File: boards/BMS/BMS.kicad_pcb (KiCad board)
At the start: 2 copper layers, 65 parts, among them IC1 ATMEGA16M1, J1 Mounting_Hole_4-40, J2 Mounting_Hole_4-40, J3 Mounting_Hole_4-40, J4 Ultrafit_4, J5 Mounting_Hole_4-40, J6 Ultrafit_4, J7 NanoFit_2, J8 Ultrafit_5, K1 G5Q-1A4-DC5-5V, P1 CONN_02X03, Q1 2N7002, T1 T_LAN_7490100111A, U1 micro-match12pin, U2 CAN_Transceiver, U3 TPS561201, U4 SN74LVC1G17, U5 AD623, U6 MCP6001, U7 LTC6820, Y1 Crystal_SMD

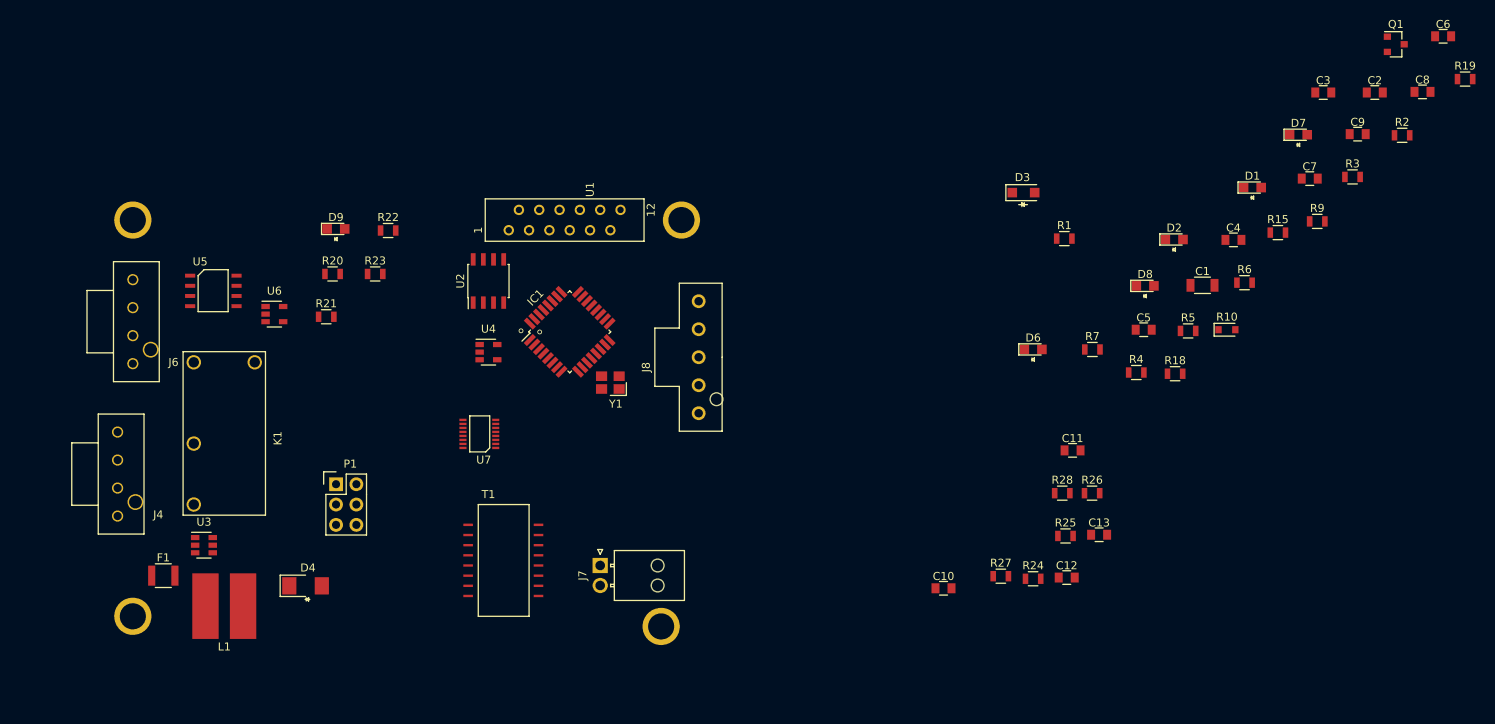
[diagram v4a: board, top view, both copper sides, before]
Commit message: BMS: Layout, tracing, and fabrication outputs
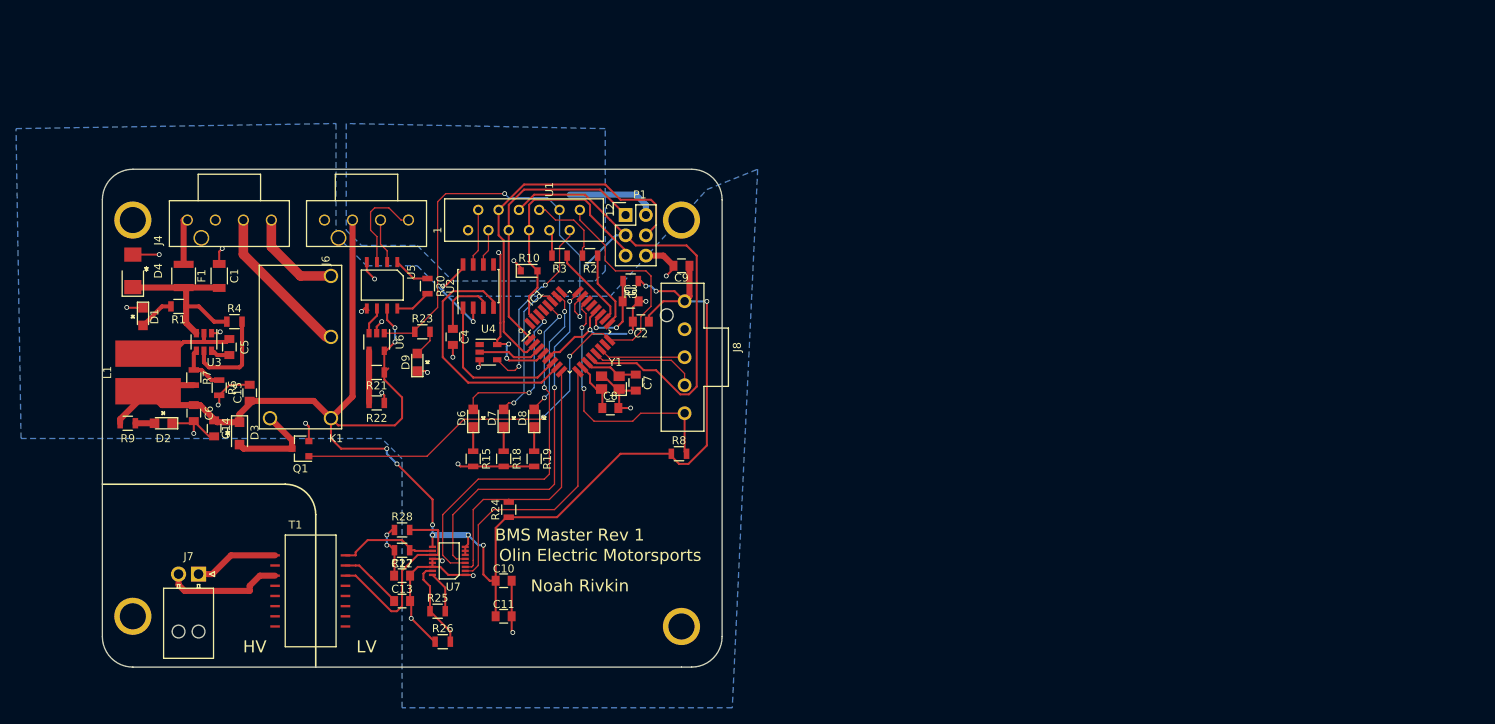
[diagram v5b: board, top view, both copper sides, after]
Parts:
- added C14: C_10uF_16V, footprints:C_0805_OEM, F.Cu at (138.4, 92.1)
- added C15: C_0.1uF, footprints:C_0805_OEM, F.Cu at (142.9, 87.6)
- added R8: R_10k, footprints:R_0805_OEM, F.Cu at (196.5, 95.2)
- moved C6 163.1 mm to (135.9, 90.2), turned to 270 degrees
- moved R9 150.8 mm to (127.6, 91.4)
- moved Q1 145.9 mm to (149.2, 94.6), turned to 180 degrees
- moved D1 139.6 mm to (129.5, 78.1), turned to 270 degrees
- moved R6 128.8 mm to (139.1, 87.0), turned to 270 degrees
- moved D2 128.4 mm to (132.1, 91.4), turned to 180 degrees
- moved R19 125.7 mm to (178.4, 95.9), turned to 270 degrees
- moved C1 122.9 mm to (139.1, 73.0), turned to 90 degrees
- moved C5 114.3 mm to (140.3, 81.9), turned to 90 degrees
- moved R4 112.9 mm to (141.0, 78.7)
- moved R7 112.4 mm to (135.9, 85.7), turned to 270 degrees
- moved R1 111.0 mm to (134.0, 76.8), turned to 180 degrees
- moved C8 108.9 mm to (188.0, 89.5)
- moved D7 105.5 mm to (174.6, 90.8), turned to 90 degrees
- moved R15 104.5 mm to (170.8, 95.9), turned to 270 degrees
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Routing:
- net VCC: track 0.00 -> 252.0 mm, vias 0 -> 15
- net GND: track 0.00 -> 118.0 mm, vias 0 -> 26
- net Shutdown_Control: track 0.00 -> 72.8 mm, vias 0 -> 2
- net SCK: track 0.00 -> 64.7 mm
- net BSPD_Current_Sense: track 0.00 -> 55.4 mm, vias 0 -> 2
- net MOSI: track 0.00 -> 47.2 mm
- net SCK_iso: track 0.00 -> 46.5 mm, vias 0 -> 2
- net CS_iso: track 0.00 -> 46.3 mm, vias 0 -> 2
- net MOSI_iso: track 0.00 -> 35.8 mm
- net MISO_iso: track 0.00 -> 35.0 mm
- net MISO: track 0.00 -> 34.7 mm
- net Net-(IC1-Pad22): track 0.00 -> 33.2 mm, vias 0 -> 2
- net RESET: track 0.00 -> 31.8 mm
- net RXCAN: track 0.00 -> 31.6 mm
- net Net-(R28-Pad2): track 0.00 -> 25.9 mm
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- added copper zone on B.Cu, net GND
- added copper zone on B.Cu, net VCC
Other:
- board outline added: 77.5 x 62.2 mm
- board text added: "BMS Master Rev 1"
- board text added: "HV"
- board text added: "LV"
- board text added: "Noah Rivkin"
- board text added: "Olin Electric Motorsports"

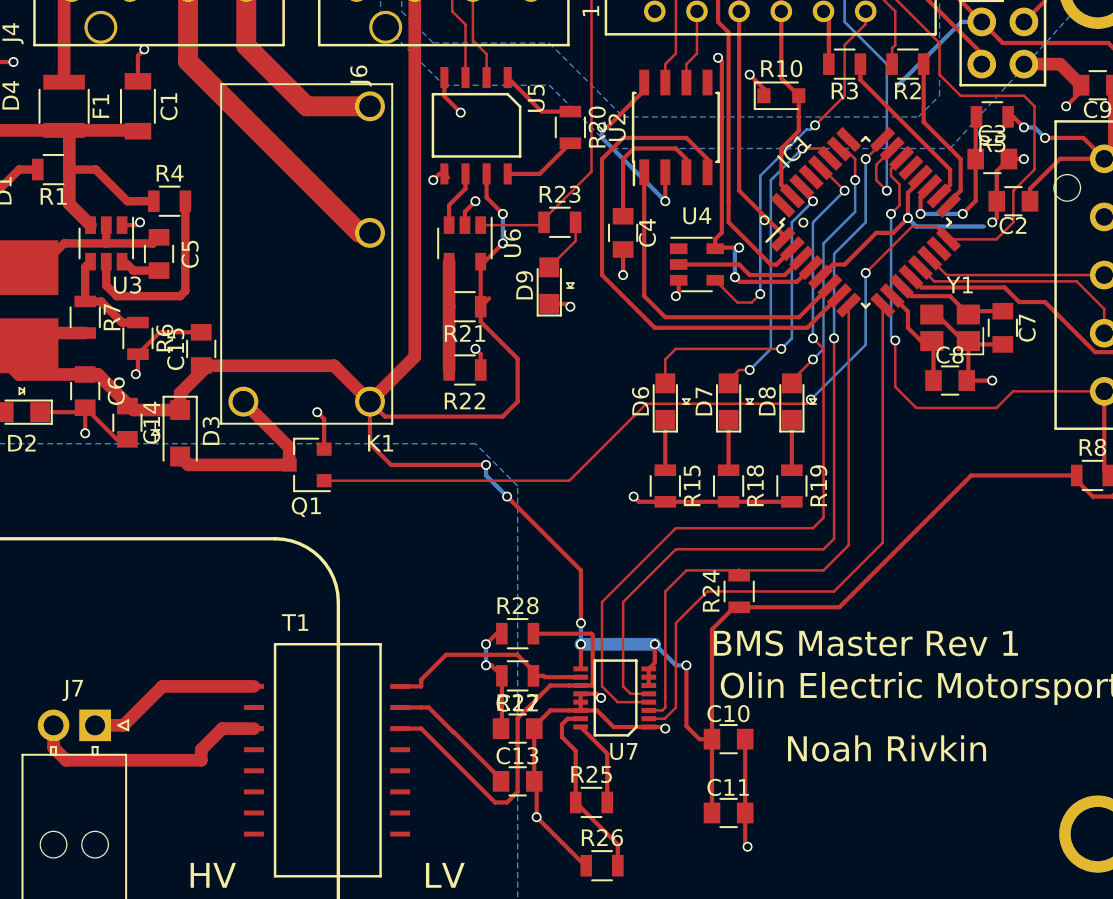
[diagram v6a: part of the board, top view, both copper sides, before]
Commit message: BMS_Slave: updated tracing/connector for temp sense
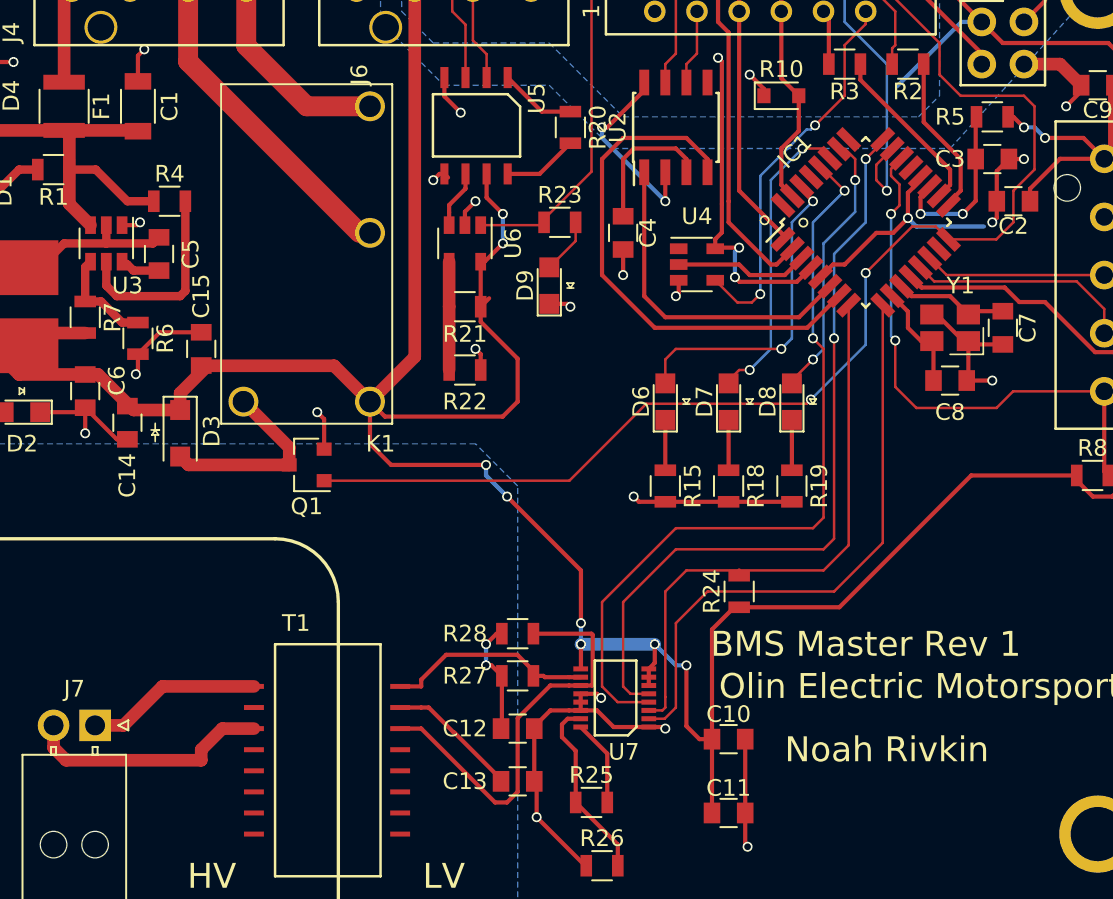
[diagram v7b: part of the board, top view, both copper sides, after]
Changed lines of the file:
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@@
     (links 155)
     (no_connects 0)
-    (area 124.384999 59.614999 202.005001 121.995001)
+    (area 113.665 53.975 206.375001 127.000001)
     (thickness 1.6)
     (drawings 24)
@@
     (tags "capacitor 0805")
     (attr smd)
-    (fp_text reference C3 (at 0 -1.5) (layer F.SilkS)
+    (fp_text reference C3 (at -2.54 0) (layer F.SilkS)
       (effects (font (size 1 1) (thickness 0.15)))
     )
@@
     (tags "capacitor 0805")
     (attr smd)
-    (fp_text reference C6 (at 0 -1.905 270) (layer F.SilkS)
+    (fp_text reference C6 (at -0.635 -1.905 270) (layer F.SilkS)
       (effects (font (size 1 1) (thickness 0.15)))
     )
@@
     (tags "capacitor 0805")
     (attr smd)
-    (fp_text reference C8 (at 0 -1.5) (layer F.SilkS)
+    (fp_text reference C8 (at 0 1.905) (layer F.SilkS)
       (effects (font (size 1 1) (thickness 0.15)))
     )
@@
     (tags "capacitor 0805")
     (attr smd)
-    (fp_text reference C12 (at 0 -1.5) (layer F.SilkS)
+    (fp_text reference C12 (at -3.175 0) (layer F.SilkS)
       (effects (font (size 1 1) (thickness 0.15)))
     )
@@
     (tags "capacitor 0805")
     (attr smd)
-    (fp_text reference C13 (at 0 -1.5) (layer F.SilkS)
+    (fp_text reference C13 (at -3.175 0) (layer F.SilkS)
       (effects (font (size 1 1) (thickness 0.15)))
     )
@@
     (tags "resistor 0805")
     (attr smd)
-    (fp_text reference R5 (at 0 -1.65 180) (layer F.SilkS)
+    (fp_text reference R5 (at 2.54 0 180) (layer F.SilkS)
       (effects (font (size 1 1) (thickness 0.15)))
     )
@@
     (tags "resistor 0805")
     (attr smd)
-    (fp_text reference R27 (at 0 -1.65 180) (layer F.SilkS)
+    (fp_text reference R27 (at 3.175 0 180) (layer F.SilkS)
       (effects (font (size 1 1) (thickness 0.15)))
     )
@@
     (tags "resistor 0805")
     (attr smd)
-    (fp_text reference R28 (at 0 -1.65) (layer F.SilkS)
+    (fp_text reference R28 (at -3.175 0) (layer F.SilkS)
       (effects (font (size 1 1) (thickness 0.15)))
     )
@@
     (tags "capacitor 0805")
     (attr smd)
-    (fp_text reference C14 (at 0 -1.5 270) (layer F.SilkS)
+    (fp_text reference C14 (at 3.175 0 270) (layer F.SilkS)
       (effects (font (size 1 1) (thickness 0.15)))
     )
@@
     (tags "capacitor 0805")
     (attr smd)
-    (fp_text reference C15 (at 0 -1.5 90) (layer F.SilkS)
-      (effects (font (size 1 1) (thickness 0.15)))
-    )
+    (fp_text reference C15 (at 3.175 0 90) (layer F.SilkS)
+      (effects (font (size 1 1) (thickness 0.15)))
+    )
